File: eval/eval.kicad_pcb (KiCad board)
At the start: 4 copper layers, 49.2 x 98 mm, 182 parts, among them CN1 XT30PW-M, J1 TC2030, Q1 BSC0702LS, Q10 2N7002, Q2 BSC0702LS, Q3 AP40P04Q, Q4 DMG2302UK-7, Q5 BSC0702LS, Q6 BSC0702LS, Q7 WSD4070DN, Q8 WSD4070DN, Q9 2N7002, U1 AP63205WU-7, U10 TPS7A2033PDBVR, U11 RCLAMP0521T-ES, U12 TPS7A2033PDBVR, U13 RCLAMP0521T-ES, U14 TLV9061xDBV, U15 TCAN1044VDRBRQ1, U16 MX74700T_C22468156, U17 MX74700T_C22468156, U18 TLV3501AIDBV, U19 TLV9062, U2 LM5148RGYR, U20 LM2903, U21 TS34031, U22 SN74LVC1G00DBV, U23 SN74LVC1G00DBV, U24 HYG015N03LS1C2, U25 HYG015N03LS1C2, U3 INA180A3, U4 HUSB238A-BB001-QN16R, U5 TS34031, U6 HS096T01H13, U7 MX74502D23_C41433189, U8 INA180A3, U9 STM32G0B1CBTx

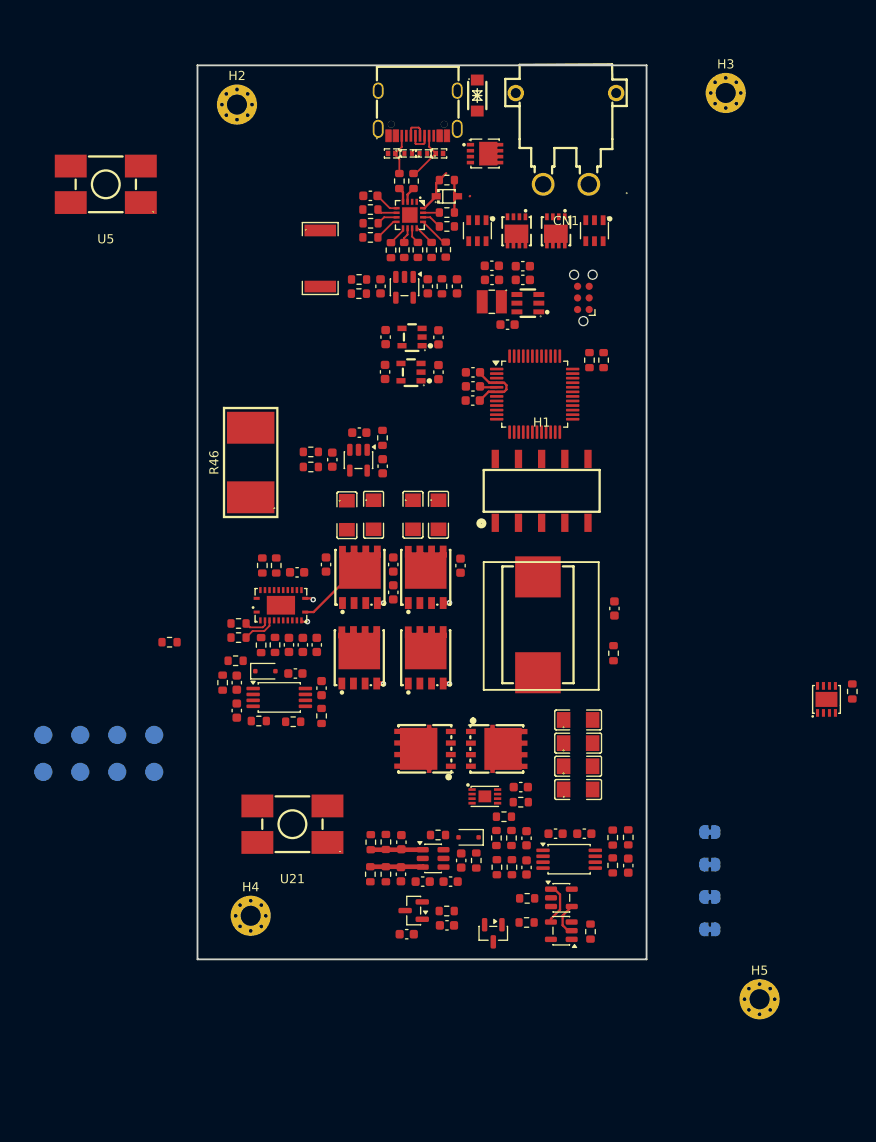
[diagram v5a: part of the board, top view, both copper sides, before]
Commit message: [trace] add high power trace
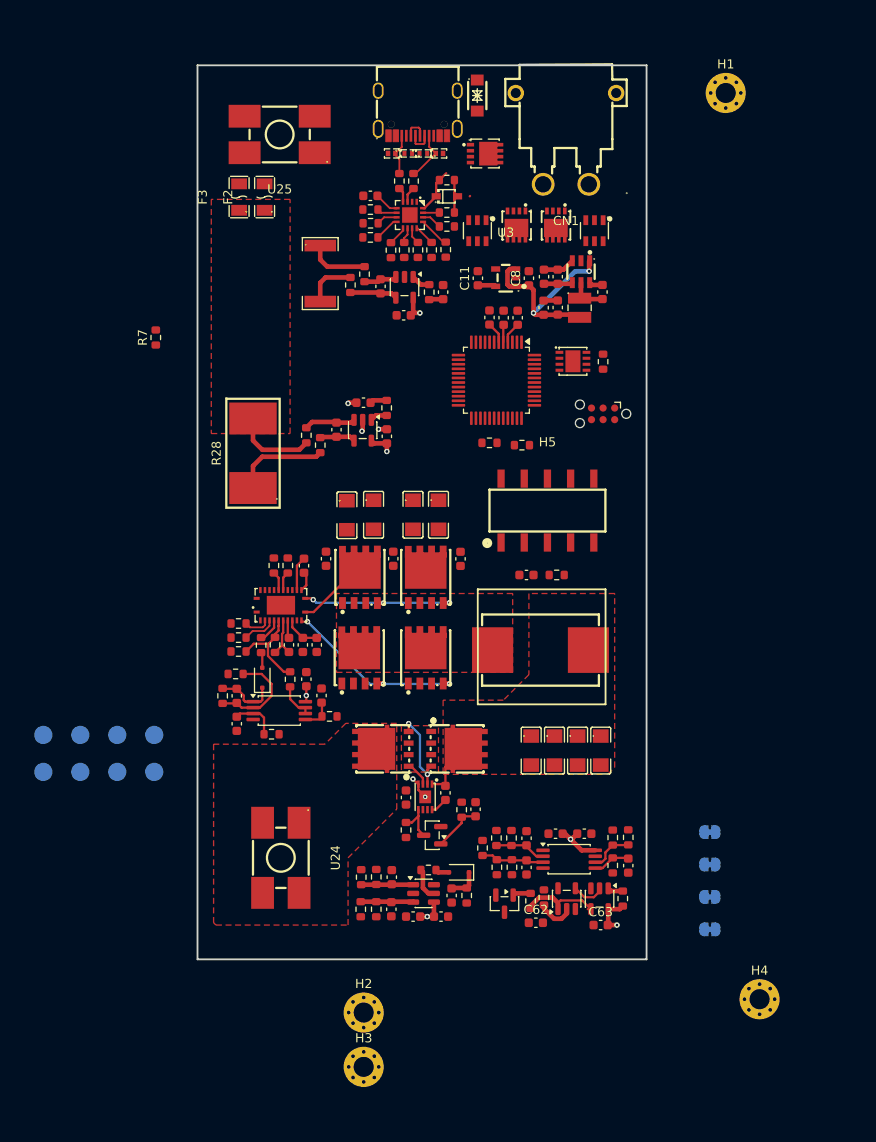
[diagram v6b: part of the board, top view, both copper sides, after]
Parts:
- removed the C26 at (60.5, 91.3)
- removed the C27 at (60.5, 87.5)
- removed the C28 at (54.6, 91.3)
- removed the C29 at (54.7, 87.5)
- removed C45: 100n, Capacitor_SMD:C_0603_1608Metric
- removed the H4 at (39.9, 150.9)
- removed the U10 at (57.4, 91.3)
- removed the U12 at (57.6, 87.5)
- added C11: 1u, Capacitor_SMD:C_0603_1608Metric, F.Cu at (64.8, 81.0)
- added C62: 100n, Capacitor_SMD:C_0603_1608Metric, F.Cu at (71.1, 151.6)
- added C63: 100n, Capacitor_SMD:C_0603_1608Metric, F.Cu at (78.2, 151.9)
- added C8: 1u, Capacitor_SMD:C_0603_1608Metric, F.Cu at (70.4, 81.0)
- added F2: JFC1206-2300FS, EasyEDA:F1206, F.Cu at (41.4, 72.1)
- added F3: JFC1206-2300FS, EasyEDA:F1206, F.Cu at (38.6, 72.1)
- added H3: MountingHole_Pad, MountingHole:MountingHole_2.2mm_M2_Pad_Via, F.Cu at (52.3, 167.4)
- added R7: 0, Resistor_SMD:R_0603_1608Metric, F.Cu at (29.5, 87.5)
- added U3: TPS7A2033PDBVR, EasyEDA:SOT-23-5_L2.9-W1.6-P0.95-LS2.8-BR, F.Cu at (67.8, 81.0)
- moved H2 100.4 mm to (52.3, 161.5)
- moved U24 76.2 mm to (43.2, 144.5), turned to -90 degrees
- moved U25 75.6 mm to (43.1, 65.3)
- moved U8 46.3 mm to (75.2, 90.1), turned to 180 degrees
- moved R13 45.3 mm to (78.5, 90.2), turned to 90 degrees
- moved R30 15.4 mm to (66.0, 99.1), turned to 0 degrees
- moved C51 15.0 mm to (56.9, 137.9), turned to -90 degrees
- moved C50 13.1 mm to (64.5, 139.2), turned to -90 degrees
- moved R47 12.9 mm to (56.9, 141.5), turned to 90 degrees
- moved J1 12.9 mm to (78.5, 95.9), turned to 180 degrees
- moved R29 11.9 mm to (69.6, 99.3), turned to 180 degrees
- moved R46 11.2 mm to (63.0, 139.3), turned to 90 degrees
- moved C12 11.0 mm to (78.4, 82.5), turned to -90 degrees
- moved R27 10.6 mm to (73.4, 113.5), turned to 0 degrees
- moved C40 10.3 mm to (70.1, 113.5), turned to 0 degrees
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- renumbered C19 to C1, C22 to C10, C14 to C12, C23 to C14, C24 to C16, C32 to C18, C30 to C19, C20 to C2, C31 to C20, C8 to C22, C9 to C23, C36 to C24, C37 to C25, C7 to C26, C12 to C27, C17 to C28, C2 to C29, C21 to C3, C33 to C30, C1 to C31, C6 to C32, C25 to C33, C10 to C34, C18 to C35, C4 to C36, C46 to C38, C5 to C39, C15 to C4, C39 to C40, C40 to C41, C41 to C42, C42 to C43, C43 to C44, C47 to C46, C48 to C47, C3 to C48, C13 to C5, C61 to C50, C50 to C51, C57 to C52, C58 to C53, C52 to C54, C59 to C55, C60 to C56, C51 to C57, C56 to C58, C54 to C59, C11 to C6, C55 to C60, C53 to C61, C38 to C7, C16 to C9, D7 to D4, D4 to D5, D5 to D6, H3 to H1, H5 to H4, H1 to H5, JP4 to JP1, JP1 to JP4, L3 to L1, L1 to L2, Q4 to Q1, Q9 to Q10, Q6 to Q2, Q1 to Q3, Q5 to Q4, Q2 to Q5, Q7 to Q6, Q8 to Q7, Q3 to Q8, Q10 to Q9, R11 to R1, R41 to R10, R42 to R11, R43 to R12, R44 to R13, R1 to R14, R2 to R15, R4 to R16, R5 to R17, R3 to R18, R13 to R19, R18 to R2, R14 to R20, R6 to R23, R7 to R24, R8 to R25, R23 to R26, R45 to R27, R46 to R28, R28 to R29, R15 to R3, R29 to R30, R26 to R31, R27 to R32, R34 to R33, R36 to R34, R30 to R35, R31 to R36, R35 to R37, R37 to R38, R38 to R39, R12 to R4, R47 to R40, R24 to R41, R33 to R42, R32 to R43, R65 to R44, R66 to R45, R64 to R46, R58 to R47, R56 to R48, R53 to R49, R10 to R5, R25 to R50, R48 to R51, R51 to R52, R52 to R53, R61 to R54, R16 to R55, R19 to R56, R54 to R57, R55 to R58, R9 to R6, R49 to R61, R50 to R62, R40 to R8, R39 to R9, TP8 to TP1, TP9 to TP2, TP6 to TP3, TP7 to TP4, TP4 to TP6, TP1 to TP7, TP2 to TP8, U9 to U1, U3 to U10, U8 to U11, U16 to U12, U17 to U13, U11 to U14, U13 to U15, U4 to U16, U24 to U17, U7 to U18, U22 to U19, U19 to U2, U23 to U20, U25 to U21, U20 to U22, U18 to U23, U5 to U24, U21 to U25, U1 to U4, U14 to U7, U15 to U8, U2 to U9
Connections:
- C51 pad 1: Net-(C50-Pad1) -> VBAT
- U21 pad 5: Net-(C50-Pad1) -> VBAT
- U21 pad 6: Net-(C50-Pad1) -> VBAT
- U21 pad 7: Net-(C50-Pad1) -> VBAT
- U21 pad 8: Net-(C50-Pad1) -> VBAT
- U21 pad 9: Net-(C50-Pad1) -> VBAT
- U25 pad 1: /power_buck/OUT_ISNS+ -> Net-(F2-Pad2)
- U25 pad 2: /power_buck/OUT_ISNS+ -> Net-(F2-Pad2)
- U25 pad 3: /power_buck/OUT_ISNS+ -> Net-(F2-Pad2)
- U25 pad 4: /power_buck/OUT_ISNS+ -> Net-(F2-Pad2)
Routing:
- net +5V: track 0.00 -> 22.6 mm, vias 0 -> 2
- net +3V3: track 10.3 -> 29.7 mm, vias 0 -> 6
- net GNDPWR: track 0.00 -> 12.9 mm, vias 0 -> 2
- net GNDA: track 0.00 -> 12.8 mm, vias 0 -> 3
- net Net-(U2A--): track 0.00 -> 11.0 mm
- net /power_buck/FB: track 0.15 -> 10.5 mm
- net VBUS: track 0.05 -> 10.3 mm
- net /power_battery/GATE: track 0.00 -> 9.39 mm, vias 0 -> 2
- net /power_buck/OUT_ISNS+: track 0.00 -> 8.99 mm
- net Net-(D1-K): track 0.00 -> 7.04 mm
- net /power_battery/vbat_none_neg: track 0.00 -> 6.93 mm
- net /power_buck/VOUT: track 0.00 -> 6.41 mm
- net /power_battery/power_on_hold: track 0.00 -> 6.40 mm
- net /power_battery/vbat_comp_thre: track 0.00 -> 5.69 mm
- net Net-(U10-+): track 0.00 -> 5.64 mm
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- added copper zone on F.Cu, net /power_buck/OUT_ISNS+
- added copper zone on F.Cu, net /power_buck/SW
- added copper zone on F.Cu, net /power_buck/VOUT
- added copper zone on In1.Cu, net GNDPWR
- added copper zone on F.Cu, net Net-(U18-SRC)
- added copper zone on F.Cu, net VBAT
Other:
- board text added: "Add via for heat"

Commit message: [trace] add copper zone for input mux and pd
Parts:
- moved C10 30.4 mm to (100.3, 95.3)
- moved C11 30.4 mm to (91.5, 95.4)
- moved C14 30.4 mm to (100.3, 98.6)
- moved C8 30.4 mm to (97.1, 95.4)
- moved C9 30.4 mm to (98.8, 95.3)
- moved U3 30.4 mm to (94.6, 95.4)
- moved C12 30.4 mm to (105.2, 96.9)
- moved C16 30.4 mm to (98.7, 98.7)
- moved L1 30.4 mm to (102.7, 98.7)
- moved U4 30.4 mm to (102.8, 94.7)
- moved U13 28.6 mm to (49.3, 71.8)
- moved C48 20.5 mm to (73.5, 71.3), turned to 90 degrees
- moved R31 19.1 mm to (76.9, 70.6)
- moved R32 19.1 mm to (75.3, 70.6)
- moved R40 19.1 mm to (77.3, 78.2)
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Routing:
- net Net-(D5-A): track 3.84 -> 0.00 mm
- net /power_usb_pd/FAULT: track 3.40 -> 0.00 mm
- net Net-(D3-C): track 5.78 -> 2.67 mm
- net Net-(U16-FLGIN): track 2.20 -> 0.00 mm
- net Net-(D2-C): track 4.60 -> 2.42 mm
- net Net-(U16-GATE): track 1.79 -> 0.00 mm
- net Net-(D5-K): track 4.96 -> 4.37 mm
- added copper zone on F.Cu, net Net-(D5-K)

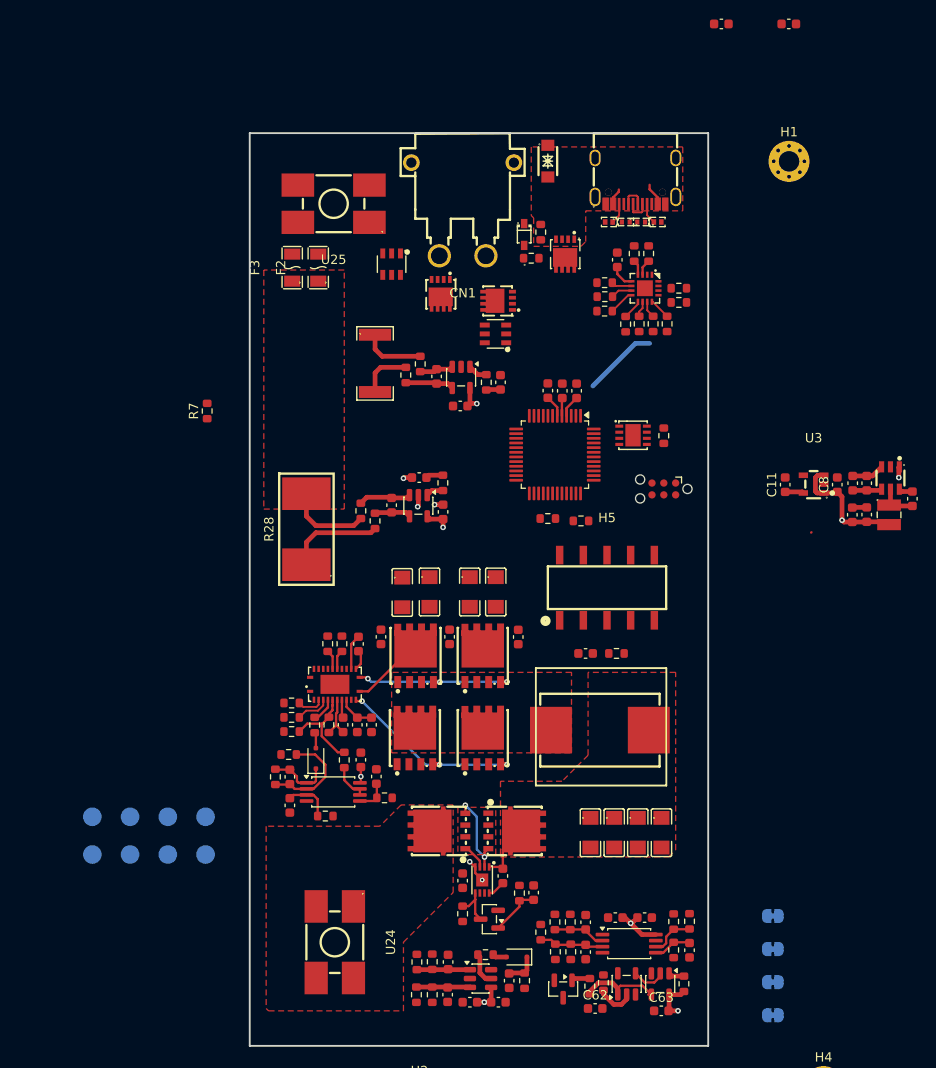
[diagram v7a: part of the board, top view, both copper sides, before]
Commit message: [sch] Remote volt-drop detect and NAND latch
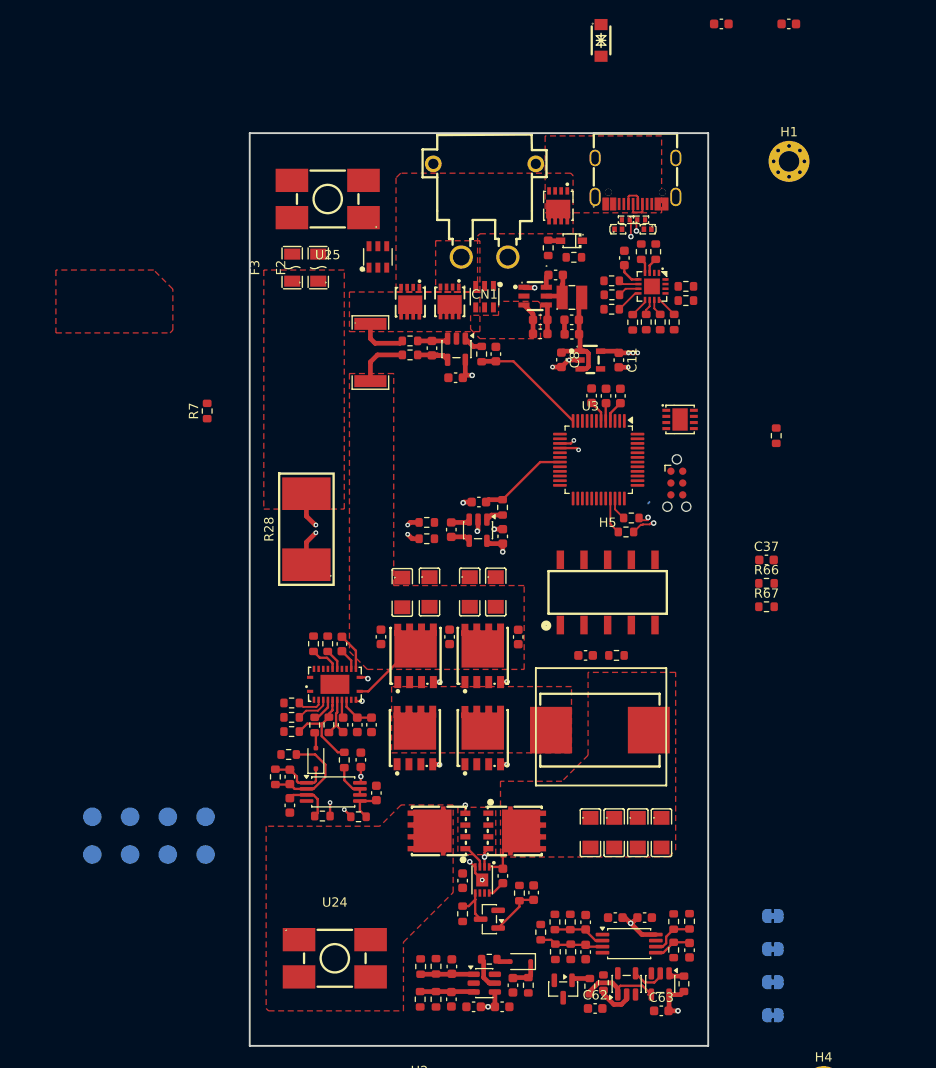
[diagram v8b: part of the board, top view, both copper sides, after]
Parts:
- added C37: 100n, Capacitor_SMD:C_0603_1608Metric, F.Cu at (89.5, 103.5)
- added R66: R_Small, Resistor_SMD:R_0603_1608Metric, F.Cu at (89.5, 106.0)
- added R67: R_Small, Resistor_SMD:R_0603_1608Metric, F.Cu at (89.5, 108.5)
- moved C12 45.2 mm to (66.9, 72.9), turned to 0 degrees
- moved U4 42.8 mm to (64.7, 75.2), turned to -90 degrees
- moved L1 41.3 mm to (68.6, 75.3), turned to 0 degrees
- moved C10 39.2 mm to (65.2, 77.7), turned to 180 degrees
- moved C14 37.9 mm to (68.6, 77.7), turned to 180 degrees
- moved C9 37.2 mm to (65.2, 79.2), turned to 180 degrees
- moved C16 35.8 mm to (68.6, 79.3), turned to 180 degrees
- moved C8 32.5 mm to (67.5, 82.0), turned to -90 degrees
- moved U3 27.4 mm to (70.6, 82.0), turned to 180 degrees
- moved C11 22.3 mm to (73.7, 82.1), turned to -90 degrees
- moved U12 15.1 mm to (47.8, 71.0), turned to 0 degrees
- moved D4 14.2 mm to (71.8, 47.8)
- moved R13 12.1 mm to (90.6, 90.2)
- moved U13 10.6 mm to (59.2, 75.2)
- moved Q6 9.44 mm to (51.3, 75.8), turned to 180 degrees
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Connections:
- net Net-(USBC1-DN1) renamed /power_usb_pd/USB-
- net Net-(USBC1-DP1) renamed /power_usb_pd/USB+
- R2 pad 1: /loop/I_CTL -> /DAC_I_SET
- R23 pad 2: /power_buck/FB -> /ADC_V_IN_MON
- R24 pad 1: /power_buck/FB -> /ADC_V_IN_MON
- R3 pad 1: /loop/V_CTL -> /DAC_V_SET
- R5 pad 2: /power_buck/FB -> /ADC_V_IN_MON
- U1 pad 11: /ADC_I_OUT_MON -> /ADC_V_IN_MON
- U1 pad 12: /ADC_V_OUT_MON -> /ADC_I_IN_MON
- U1 pad 13: /ADC_I_IN_MON -> /ADC_NTC_0
- U1 pad 14: /ADC_V_IN_MON -> /ADC_NTC_1
- U1 pad 19: unconnected-(U1-PB0-Pad19) -> /ADC_I_OUT_MON
- U1 pad 20: unconnected-(U1-PB1-Pad20) -> /ADC_V_OUT+_MON
- U1 pad 21: unconnected-(U1-PB2-Pad21) -> /ADC_V_OUT-_MON
- U9 pad 6: /power_buck/FB -> /ADC_V_IN_MON
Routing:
- net /power_usb_pd/USB-: track 2.71 -> 38.6 mm, vias 0 -> 2
- net /power_usb_pd/USB+: track 2.66 -> 37.3 mm, vias 0 -> 2
- net /ADC_I_IN_MON: track 1.54 -> 12.5 mm
- net /power_buck/FB: track 10.5 -> 0.00 mm
- net /ADC_V_IN_MON: track 0.00 -> 10.5 mm
- net +5V: track 22.6 -> 12.6 mm, vias 2 -> 1
- net /ADC_I_OUT_MON: track 1.87 -> 9.70 mm
- net /power_buck/OUT_ISNS+: track 8.99 -> 15.0 mm, vias 0 -> 2
- net GNDPWR: track 12.9 -> 17.7 mm, vias 2 -> 4
- net GNDA: track 12.8 -> 17.1 mm, vias 3 -> 6
- net Net-(D5-K): track 4.37 -> 0.14 mm
- net /USB_D-: track 0.00 -> 3.94 mm
- net Net-(U10-+): track 5.64 -> 2.15 mm
- net /DAC_V_SET: track 0.00 -> 3.14 mm, vias 0 -> 2
- net /DAC_I_SET: track 0.00 -> 3.08 mm, vias 0 -> 2
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- added copper zone on F.Cu, net /power_buck/IN_ISNS-
- added copper zone on F.Cu, net /power_dc_in/VDC
- added copper zone on F.Cu, net /power_mux/INPUT_A
- added copper zone on F.Cu, net VBUS
